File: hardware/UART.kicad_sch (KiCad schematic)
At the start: 9 parts, among them J6 DB9_Female_MountingHoles, U14 MAX202

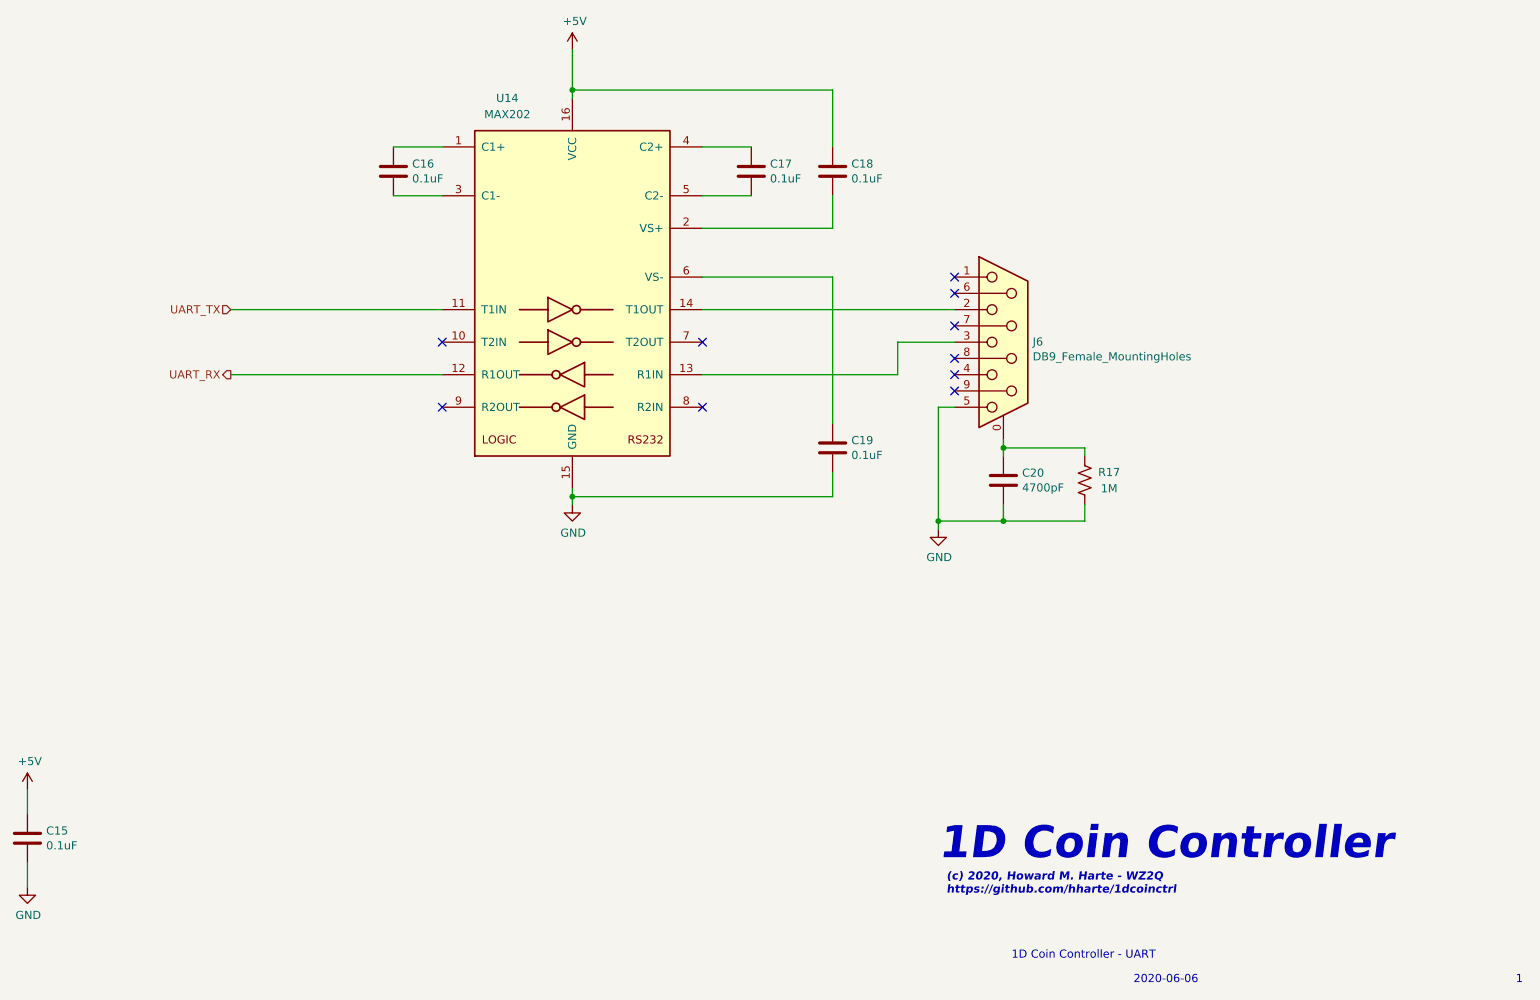
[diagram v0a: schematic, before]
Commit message: Issue 3:
* Remove barrel jack, replace with 4-position terminal block with
  provision for +/- 130VDC input in case the user already has an
  appropriate power supply and does not want the on-board
  DC-DC converter.  Note: 130V DC-DC converter PS2, relay
  K8, C14, D10, and R16 must be omitted during assembly.
* Add bi-color LEDs for line status.
  Green=Off-hook, normal polarity.
  Red=Off-hook, reverse polarity.
  Off=on-hook.
* Add header for FTDI USB UART, if user does not RS-232 UART levels.
  To use the FTDI header, do not populate U1 and other components on
  pp. 3 of the schematic.
* Remove i2c I/O expander and use PIC GPIOs directly.
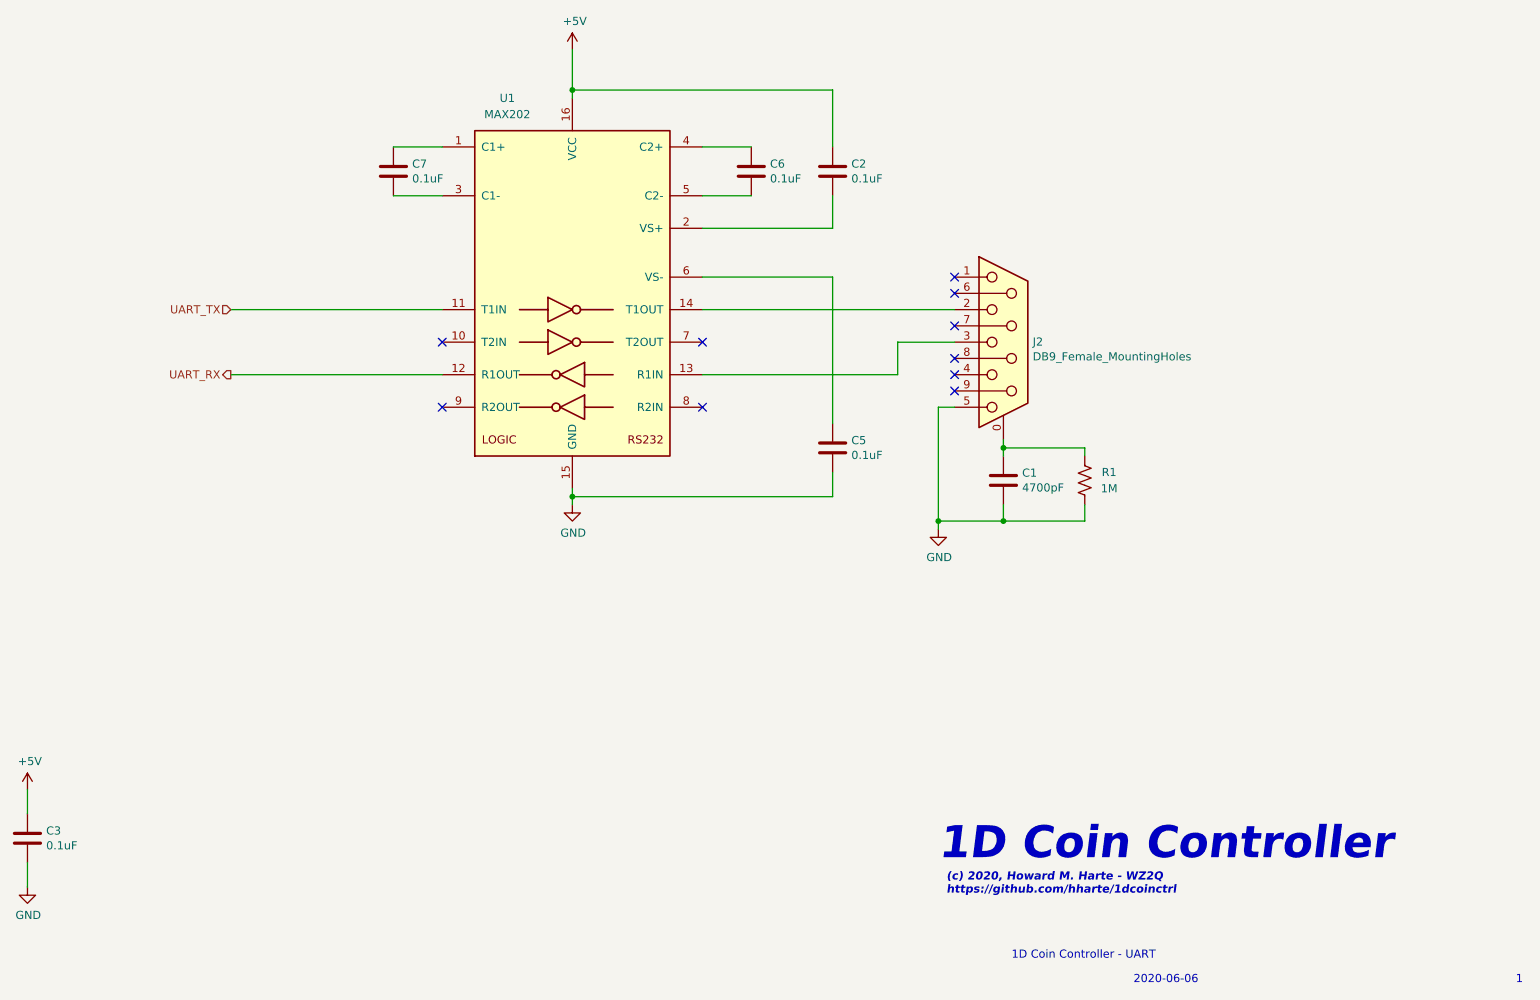
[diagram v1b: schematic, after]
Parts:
- renumbered C20 to C1, C18 to C2, C15 to C3, C19 to C5, C17 to C6, C16 to C7, J6 to J2, R17 to R1, U14 to U1
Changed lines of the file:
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@@
   (symbol (lib_id "Connector:DB9_Female_MountingHoles") (at 189.23 93.98 0) (unit 1)
     (in_bom yes) (on_board yes)
-    (property "Reference" "J6" (id 0) (at 193.802 93.9292 0)
+    (property "Reference" "J2" (id 0) (at 193.802 93.9292 0)
       (effects (font (size 1.27 1.27)) (justify left))
     )
@@
   (symbol (lib_id "Interface_UART:MAX202") (at 121.92 86.36 0) (unit 1)
     (in_bom yes) (on_board yes)
-    (property "Reference" "U14" (id 0) (at 111.76 55.88 0))
+    (property "Reference" "U1" (id 0) (at 111.76 55.88 0))
     (property "Value" "MAX202" (id 1) (at 111.76 58.42 0))
     (property "Footprint" "Package_DIP:DIP-16_W7.62mm" (id 2) (at 123.19 113.03 0)
@@
   (symbol (lib_id "Device:C") (at 36.83 171.45 0) (unit 1)
     (in_bom yes) (on_board yes)
-    (property "Reference" "C15" (id 0) (at 39.751 170.2816 0)
+    (property "Reference" "C3" (id 0) (at 39.751 170.2816 0)
       (effects (font (size 1.27 1.27)) (justify left))
     )
@@
   (symbol (lib_id "Device:C") (at 149.86 67.31 0) (unit 1)
     (in_bom yes) (on_board yes)
-    (property "Reference" "C17" (id 0) (at 152.781 66.1416 0)
+    (property "Reference" "C6" (id 0) (at 152.781 66.1416 0)
       (effects (font (size 1.27 1.27)) (justify left))
     )
@@
   (symbol (lib_id "Device:C") (at 93.98 67.31 0) (unit 1)
     (in_bom yes) (on_board yes)
-    (property "Reference" "C16" (id 0) (at 96.901 66.1416 0)
+    (property "Reference" "C7" (id 0) (at 96.901 66.1416 0)
       (effects (font (size 1.27 1.27)) (justify left))
     )
@@
   (symbol (lib_id "Device:C") (at 162.56 67.31 0) (unit 1)
     (in_bom yes) (on_board yes)
-    (property "Reference" "C18" (id 0) (at 165.481 66.1416 0)
+    (property "Reference" "C2" (id 0) (at 165.481 66.1416 0)
       (effects (font (size 1.27 1.27)) (justify left))
     )
@@
   (symbol (lib_id "Device:C") (at 162.56 110.49 0) (unit 1)
     (in_bom yes) (on_board yes)
-    (property "Reference" "C19" (id 0) (at 165.481 109.3216 0)
+    (property "Reference" "C5" (id 0) (at 165.481 109.3216 0)
       (effects (font (size 1.27 1.27)) (justify left))
     )
@@
   (symbol (lib_id "Device:C") (at 189.23 115.57 0) (unit 1)
     (in_bom yes) (on_board yes)
-    (property "Reference" "C20" (id 0) (at 192.151 114.4016 0)
+    (property "Reference" "C1" (id 0) (at 192.151 114.4016 0)
       (effects (font (size 1.27 1.27)) (justify left))
     )
@@
   (symbol (lib_id "Device:R_US") (at 201.93 115.57 0) (unit 1)
     (in_bom yes) (on_board yes)
-    (property "Reference" "R17" (id 0) (at 205.74 114.3 0))
+    (property "Reference" "R1" (id 0) (at 205.74 114.3 0))
     (property "Value" "1M" (id 1) (at 205.74 116.84 0))
     (property "Footprint" "Resistor_THT:R_Axial_DIN0207_L6.3mm_D2.5mm_P7.62mm_Horizontal" (id 2) (at 202.946 115.824 90)

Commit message: Issue 4: Switch from PIC to AVR128DA28 MCU.
    * The AVR128DA28 is supported by the Arduino IDE.
    * Simpler UPDI programming.
    * Update to KiCAD 8.0.1
    * Fix footprint outline for IA1224S DC-DC converter.
    * Add initial Arduino firmware for AVR128DA28 MCU.
    * Move Earth Ground hole.
    * Add jumpers for UART and UPDI configuration.
    * Add 3D-printable end caps for Hammond enclosure.
    * Geographical reannotate PCB.
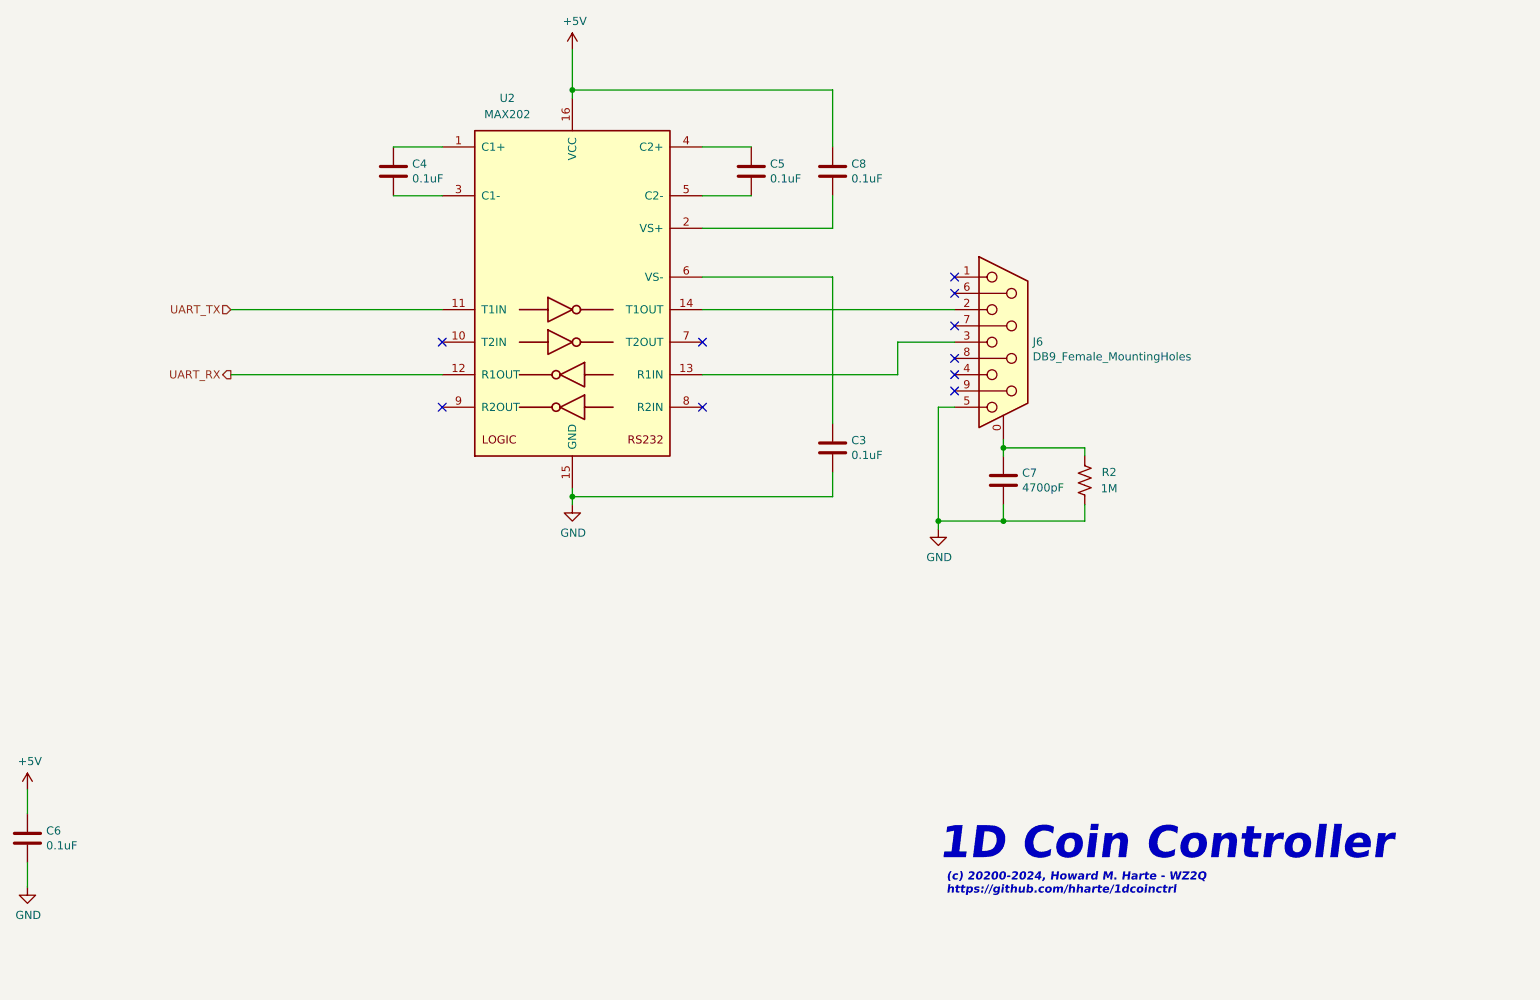
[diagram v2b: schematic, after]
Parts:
- C3: renamed from C5; Digi-Key_PN (none) -> 56-K104M15X7RF5TL2CT-ND; MPN (none) -> K104M15X7RF5TL2
- C4: renamed from C7; Digi-Key_PN (none) -> 56-K104M15X7RF5TL2CT-ND; MPN (none) -> K104M15X7RF5TL2
- C5: renamed from C6; Digi-Key_PN (none) -> 56-K104M15X7RF5TL2CT-ND; MPN (none) -> K104M15X7RF5TL2
- C6: renamed from C3; Digi-Key_PN (none) -> 56-K104M15X7RF5TL2CT-ND; MPN (none) -> K104M15X7RF5TL2
- C7: renamed from C1; Digi-Key_PN (none) -> 1288PH-ND; MPN (none) -> S472M39Z5UN63J5R
- C8: renamed from C2; Digi-Key_PN (none) -> 56-K104M15X7RF5TL2CT-ND; MPN (none) -> K104M15X7RF5TL2
- J6: renamed from J2; Digi-Key_PN (none) -> A23303-ND; MPN (none) -> 747844-4
- R2: renamed from R1; Digi-Key_PN (none) -> S1MHCT-ND; MPN (none) -> CFM12JT1M00
- U2: renamed from U1; Digi-Key_PN (none) -> HIN232CPZ-ND; MPN (none) -> HIN232CPZ
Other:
- note added: "(c) 20200-2024, Howard M. Harte - WZ2Q https://github.com/hharte/1dcoinctrl"
- note removed: "(c) 2020, Howard M. Harte - WZ2Q https://github.com/hharte/1dcoinctrl"
- note removed: "1"
- note removed: "1D Coin Controller - UART"
- note removed: "2020-06-06"
- title: (none) -> 1D Coin Controller - UART
